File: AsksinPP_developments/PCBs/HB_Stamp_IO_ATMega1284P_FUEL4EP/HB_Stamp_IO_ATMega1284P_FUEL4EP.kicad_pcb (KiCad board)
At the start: 2 copper layers, 22 x 40 mm, 35 parts, among them J1 Power, J2 FTDI Debuger, J3 ISP Programmer, J4 IO1, J5 IO2, J6 IO3, U1 ATmega1284P-AU, U2 TPS61221DCK

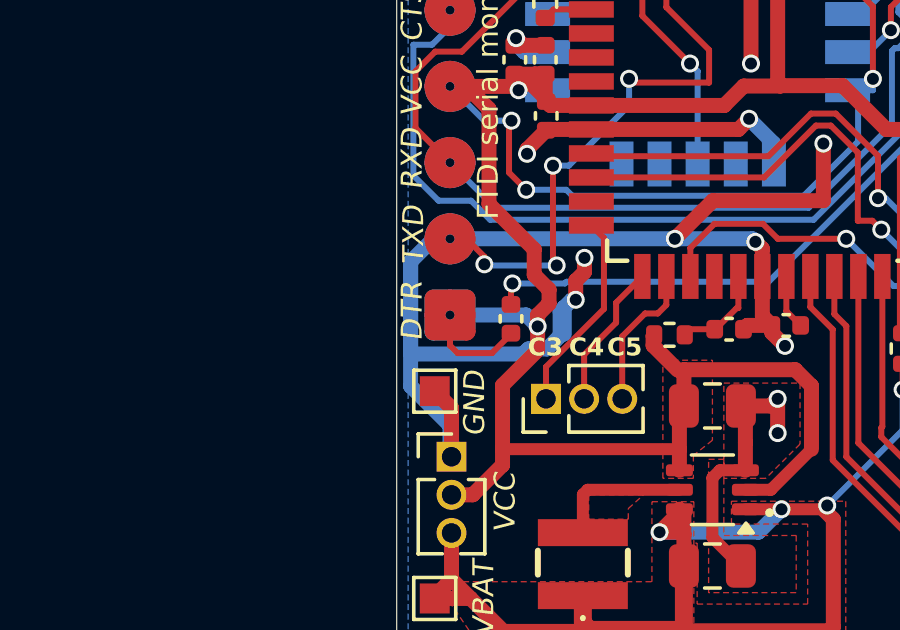
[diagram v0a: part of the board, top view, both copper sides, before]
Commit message: PCBs: updated some JLCPCB manufacturing data after trial-order
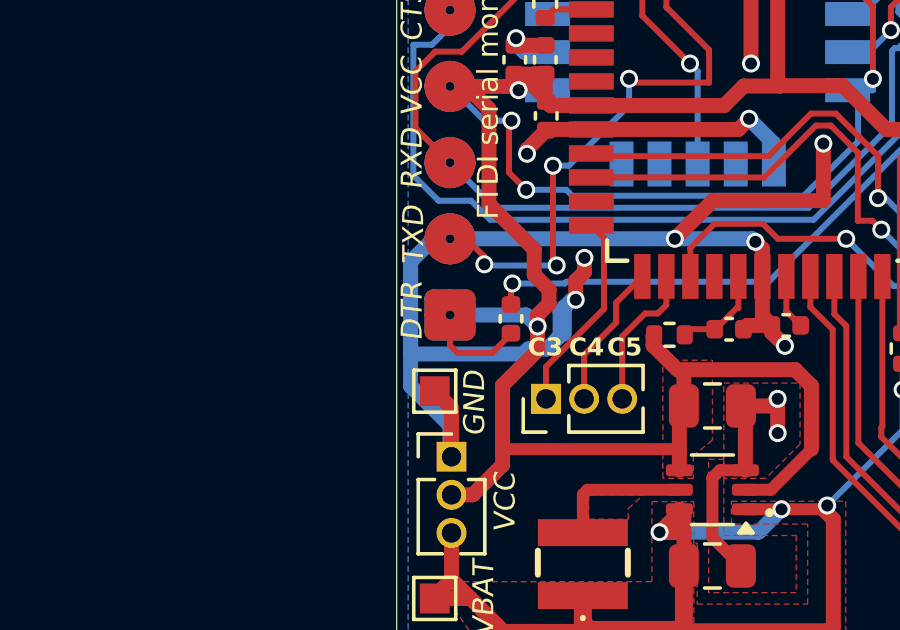
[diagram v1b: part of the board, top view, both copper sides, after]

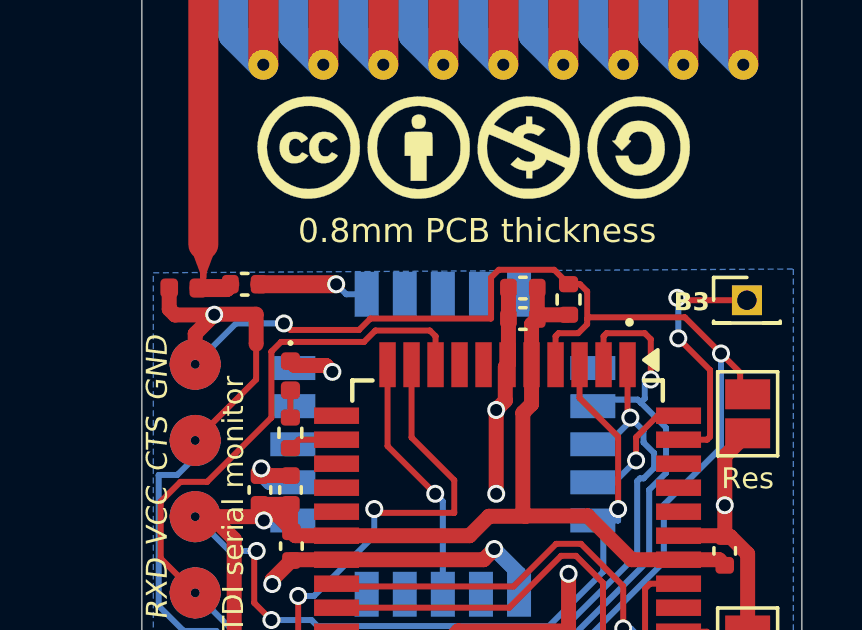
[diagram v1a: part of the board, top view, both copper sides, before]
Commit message: PCBs/HB_Stamp_IO_ATMega1284P_FUEL4EP: added test point TP3 (XTAL1)
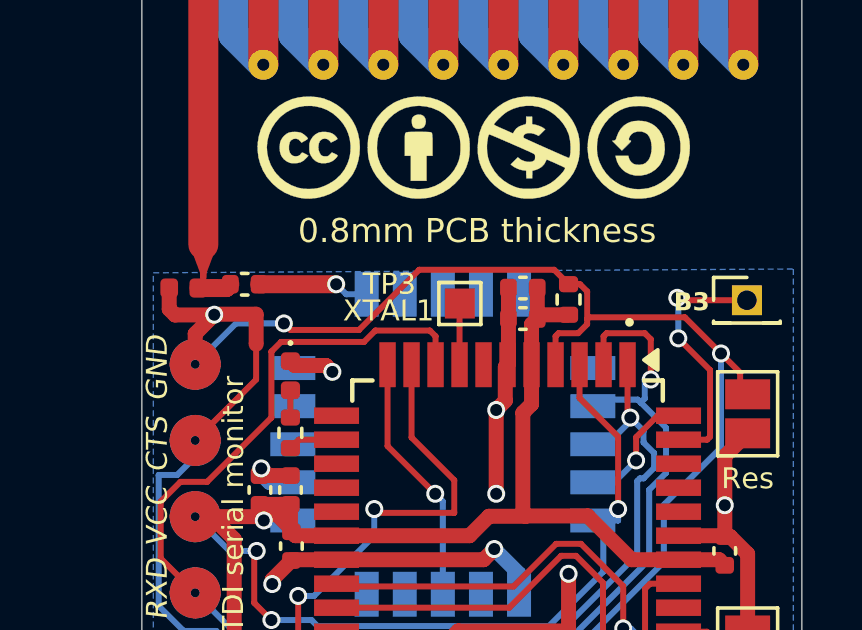
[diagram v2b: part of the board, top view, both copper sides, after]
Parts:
- added TP3: ext. clock input, TestPoint:TestPoint_Pad_1.0x1.0mm, F.Cu at (10.6, -25.9)
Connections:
- U1 pad 8: unconnected-(U1-XTAL1-Pad8) -> Net-(U1-XTAL1)
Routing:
- net Net-(U1-XTAL1): track 0.00 -> 2.03 mm
- net /RSETB: track 49.4 -> 48.6 mm
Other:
- board text added: "Version 1.1 - 05/2025 (KiCAD 8)"
- board text added: "XTAL1"
- board text added: "eByte E07-900MM10S"
- board text removed: "Version 1.0 - 02/2025 (KiCAD 8)"
